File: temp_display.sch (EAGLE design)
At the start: 63 parts, among them IC2 ATMEGA168PROUND, Q1 2N2907, T1 BC547

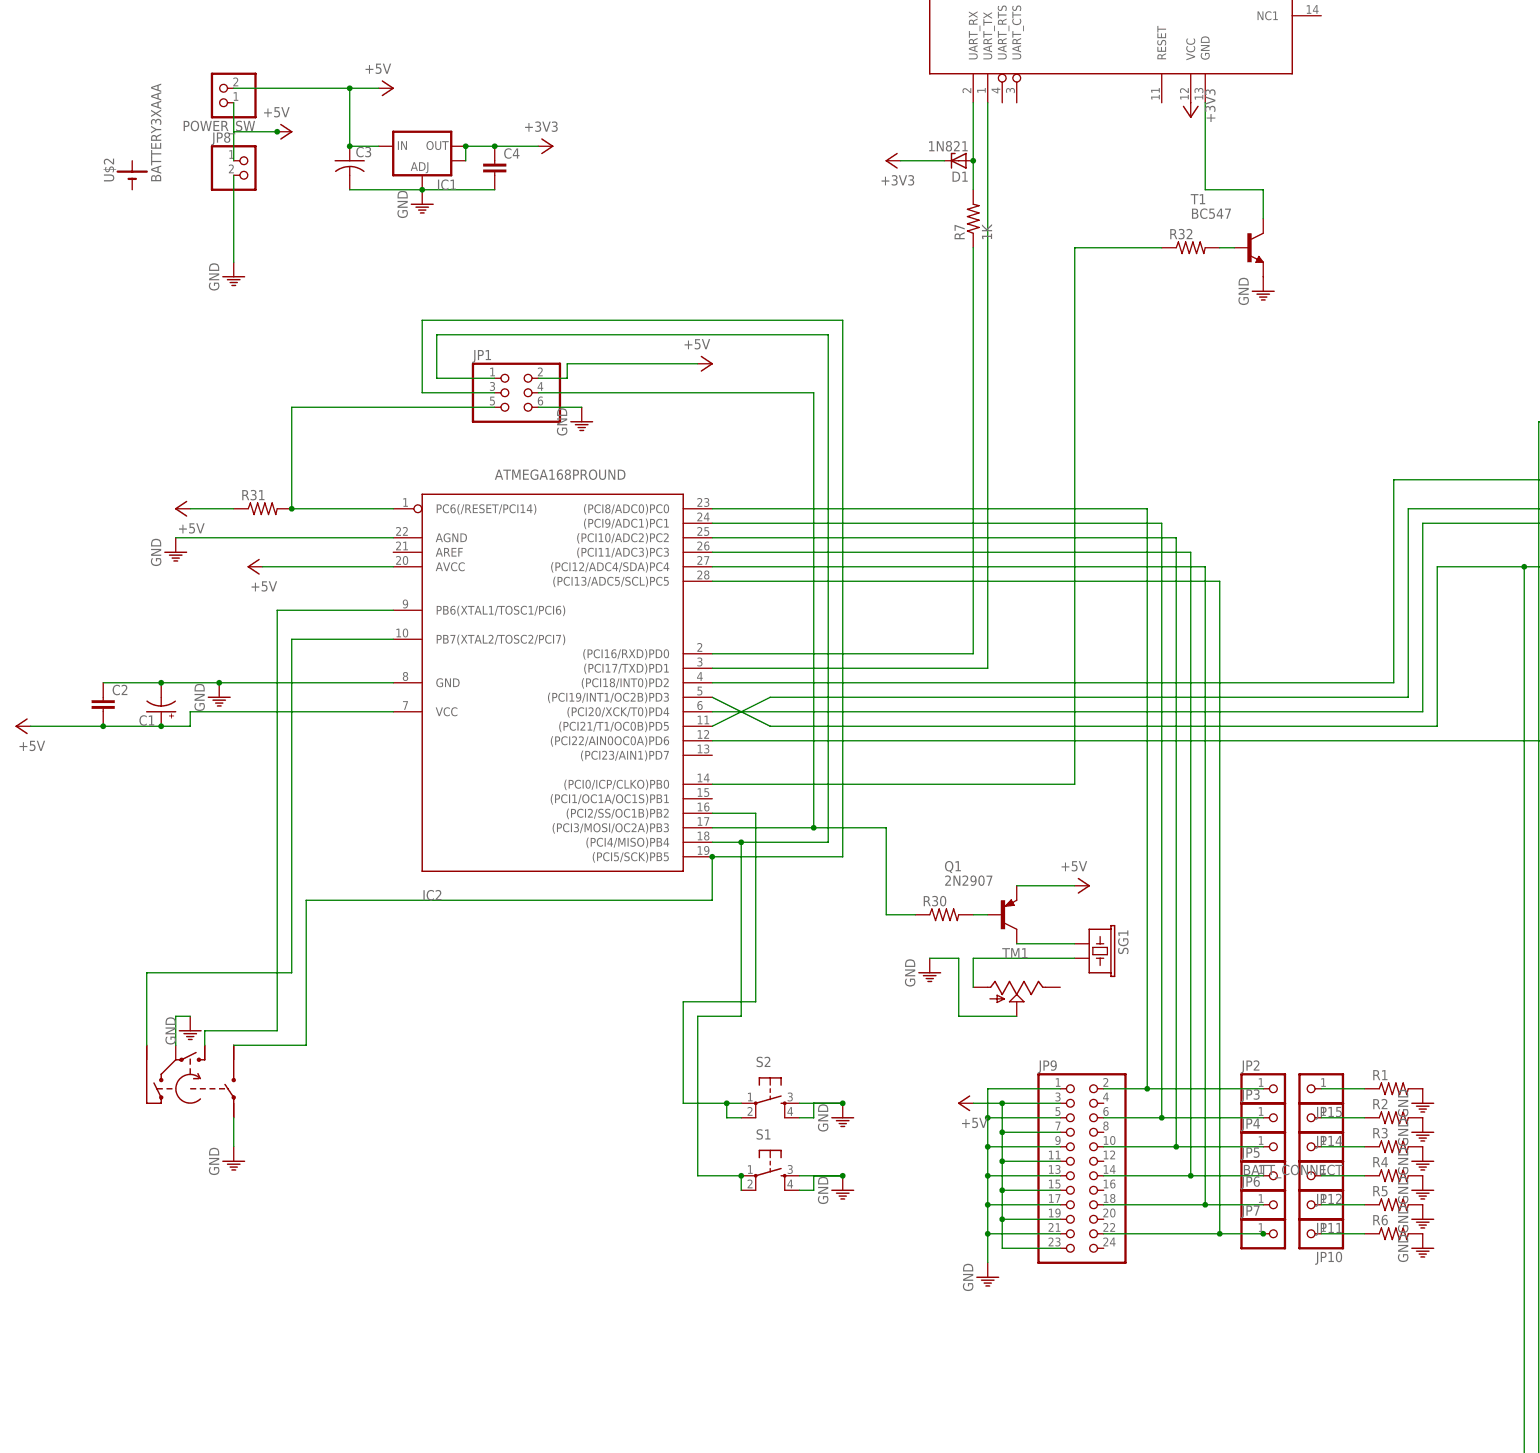
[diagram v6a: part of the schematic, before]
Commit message: Reworked the schematic to allow adding an external oscillator. Still need to build this on the proto board.
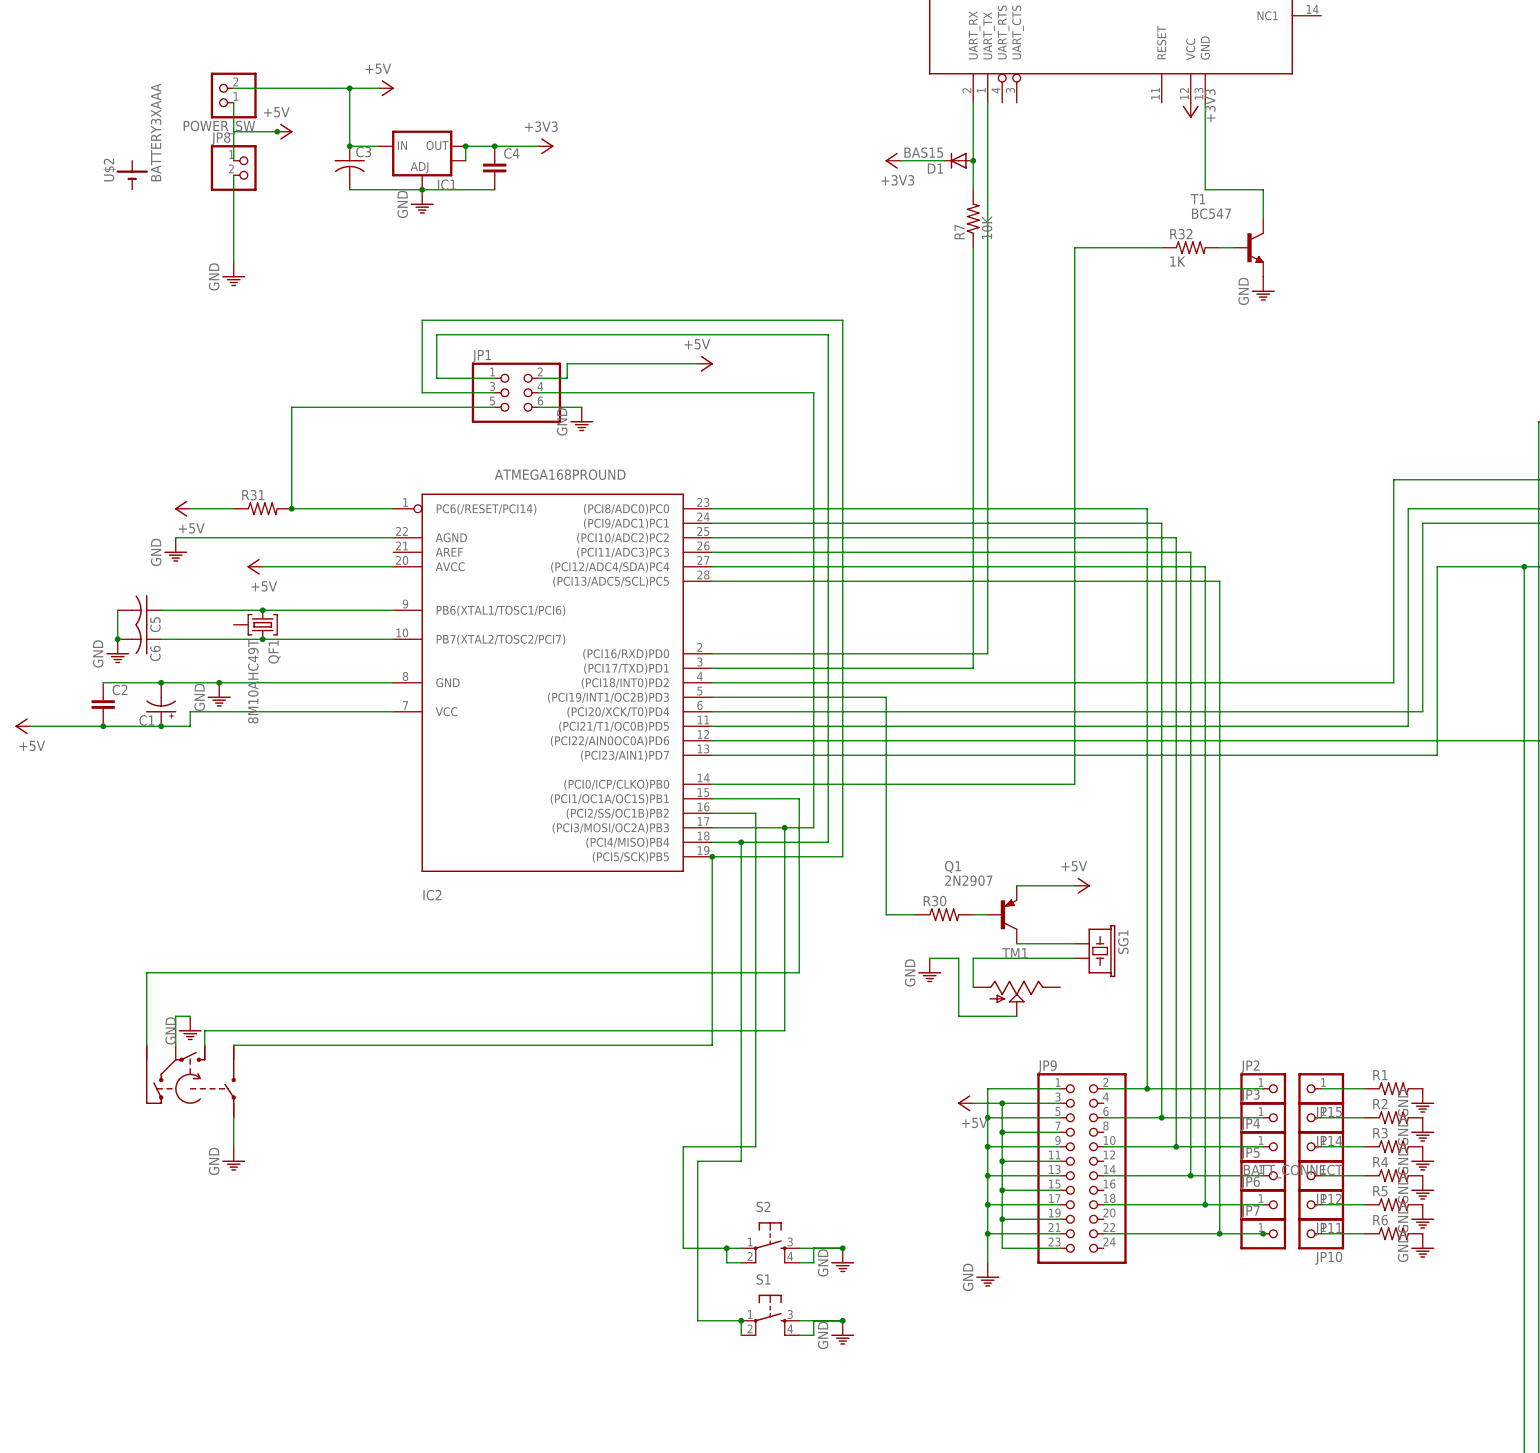
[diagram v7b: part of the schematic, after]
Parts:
- added C5, C6: (no value), resistor:C-US025-024X044
- added QF1: 8M10AHC49T, crystal:8M10AHC49T
- D1: value 1N821 -> BAS15; device diode:1N821 -> diode:BAS15
- R30: device resistor:R-US_0207/10 -> resistor:R-US_0204/2V
- R32: value (none) -> 1K
- R7: value 1K -> 10K
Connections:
- removed net N$34: IC2.(PCI3/MOSI/OC2A)PB3, JP1.4, R30.1
- new net N$10: IC2.(PCI19/INT1/OC2B)PD3, R30.1
- new net N$11: C5.1, IC2.PB6(XTAL1/TOSC1/PCI6), QF1.1
- new net N$12: C6.1, IC2.PB7(XTAL2/TOSC2/PCI7), QF1.3
- net GND: now also C5.2, C6.2
- net N$31: now also IC2.(PCI3/MOSI/OC2A)PB3, JP1.4; no longer IC2.PB6(XTAL1/TOSC1/PCI6)
- net N$41: now also IC2.(PCI1/OC1A/OC1S)PB1; no longer IC2.PB7(XTAL2/TOSC2/PCI7)
- net OE: now also IC2.(PCI23/AIN1)PD7; no longer IC2.(PCI19/INT1/OC2B)PD3
- net SERIAL_RX: now also IC2.(PCI17/TXD)PD1; no longer IC2.(PCI16/RXD)PD0
- net SERIAL_TX: now also IC2.(PCI16/RXD)PD0; no longer IC2.(PCI17/TXD)PD1
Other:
- moved on the sheet: S1, S2

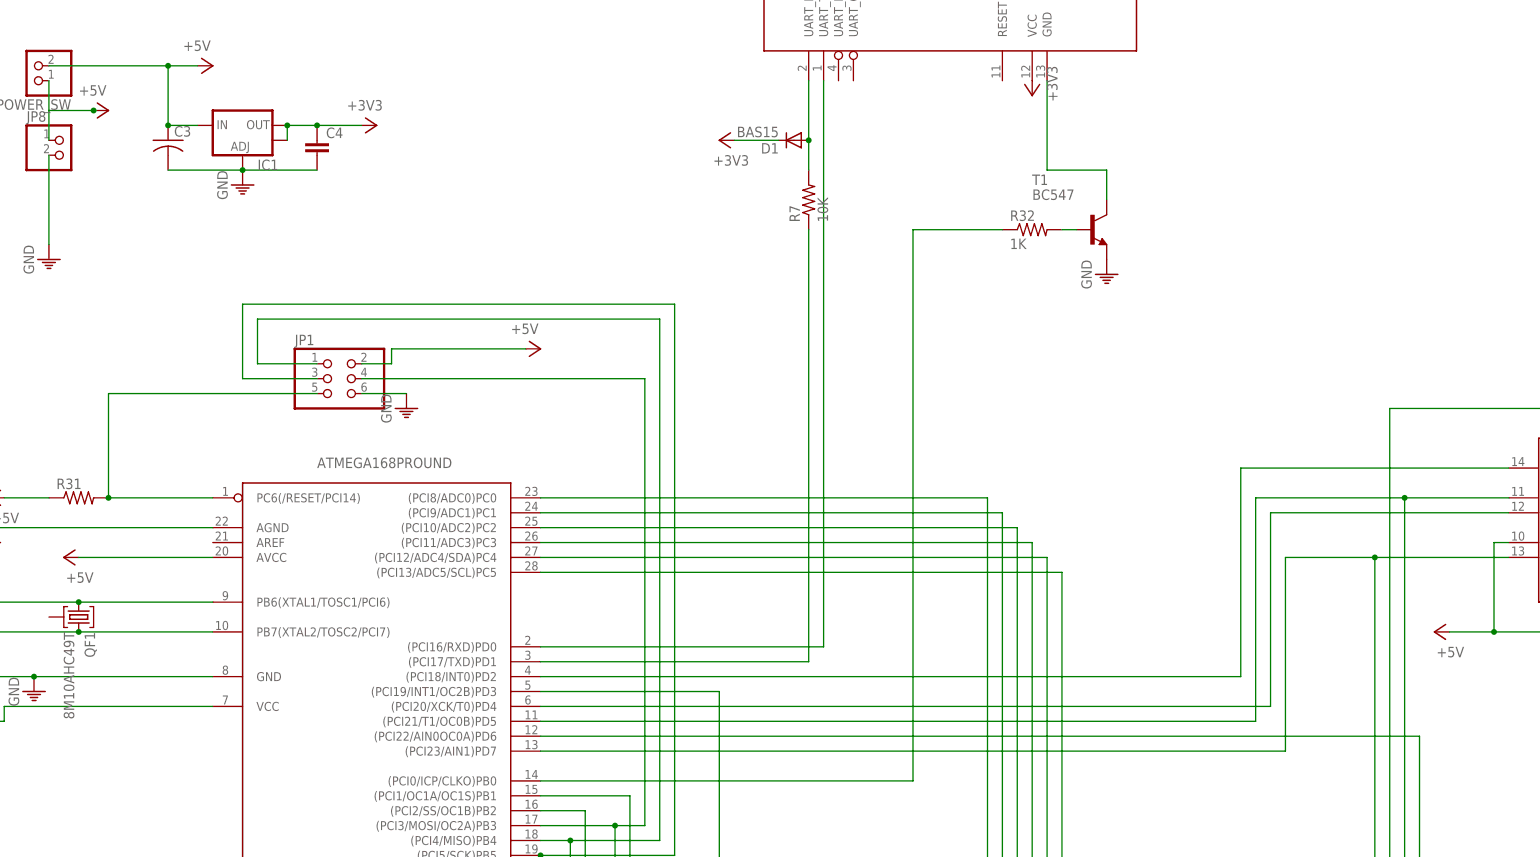
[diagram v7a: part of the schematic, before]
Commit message: Now shutting down the display during isploading. But the system isn't stable anymore.
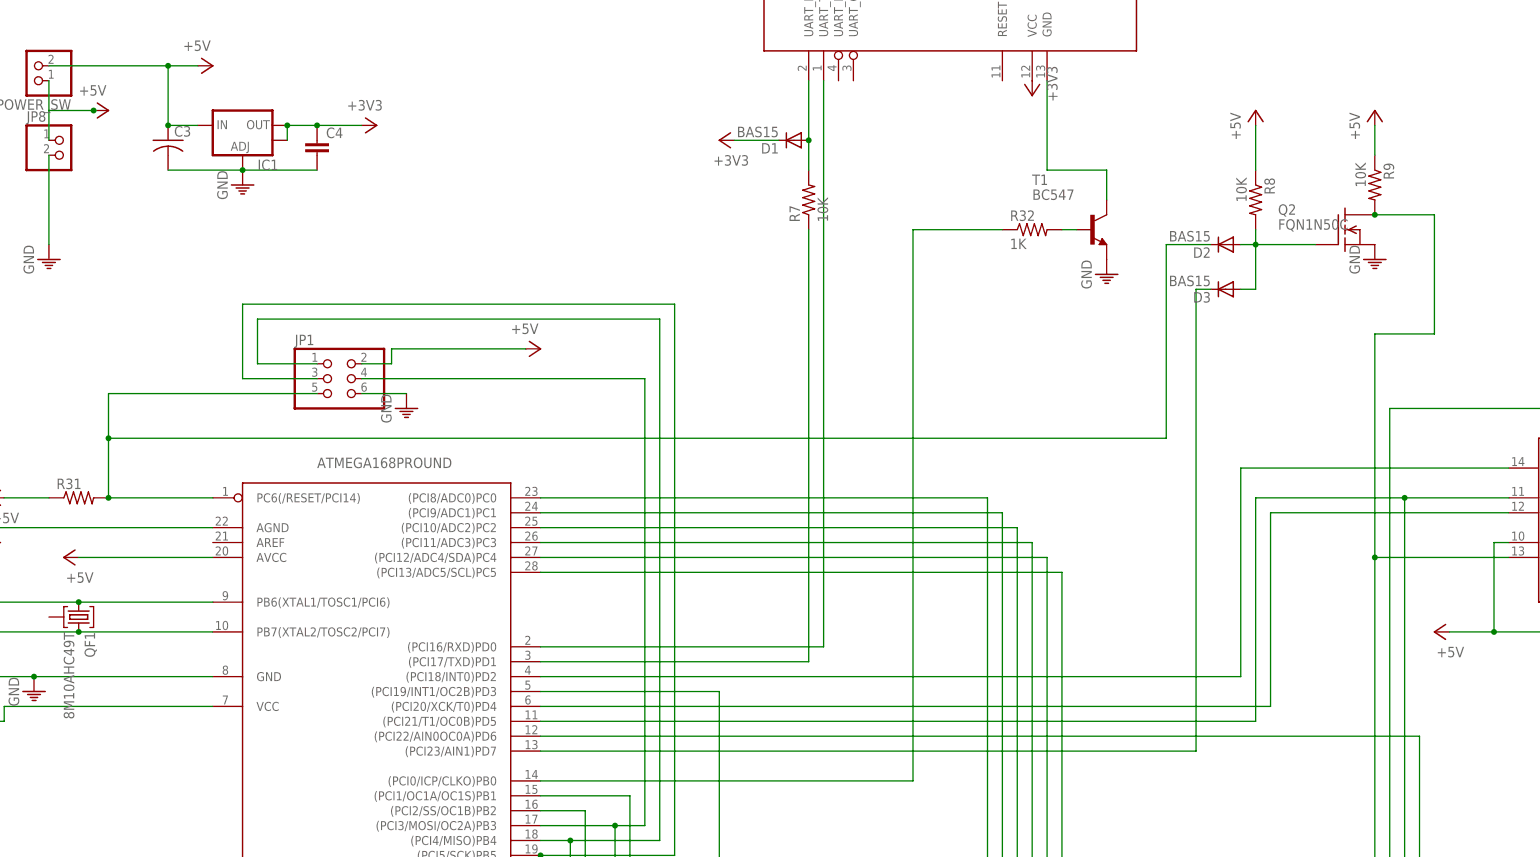
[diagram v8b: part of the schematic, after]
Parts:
- added D2, D3: BAS15, diode:BAS15
- added Q2: FQN1N50C, adafruit:FQN1N50C
- added R8, R9: 10K, resistor:R-US_0204/7
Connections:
- new net N$13: D3.C, IC2.(PCI23/AIN1)PD7
- new net N$14: D2.A, D3.A, Q2.G, R8.2
- net +5: no longer SR1.MR, SR1.VCC
- net +5V: now also R8.1, R9.1, SR1.MR, SR1.VCC
- net GND: now also Q2.S
- net OE: now also Q2.D, R9.2; no longer IC2.(PCI23/AIN1)PD7
- net RESET: now also D2.C
